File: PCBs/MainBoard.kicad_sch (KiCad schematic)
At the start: 46 parts, among them IC1 PASCO2V01BUMA1, J1 USB_C_Receptacle, J2 Conn_01x12_FPC_0.5mm, J3 Qwiic_RA, J4 SM06B-GHS-TB, SW1 PTH_RA_h7.5mm, SW2 SMD_4.6x2.8mm_h2.5mm, SW3 SMD_4.6x2.8mm_h2.5mm, U1 TVS_ESD_USB, U2 ESP32-S3-MINI, U3 AP3012, U4 AP2112K-3.3

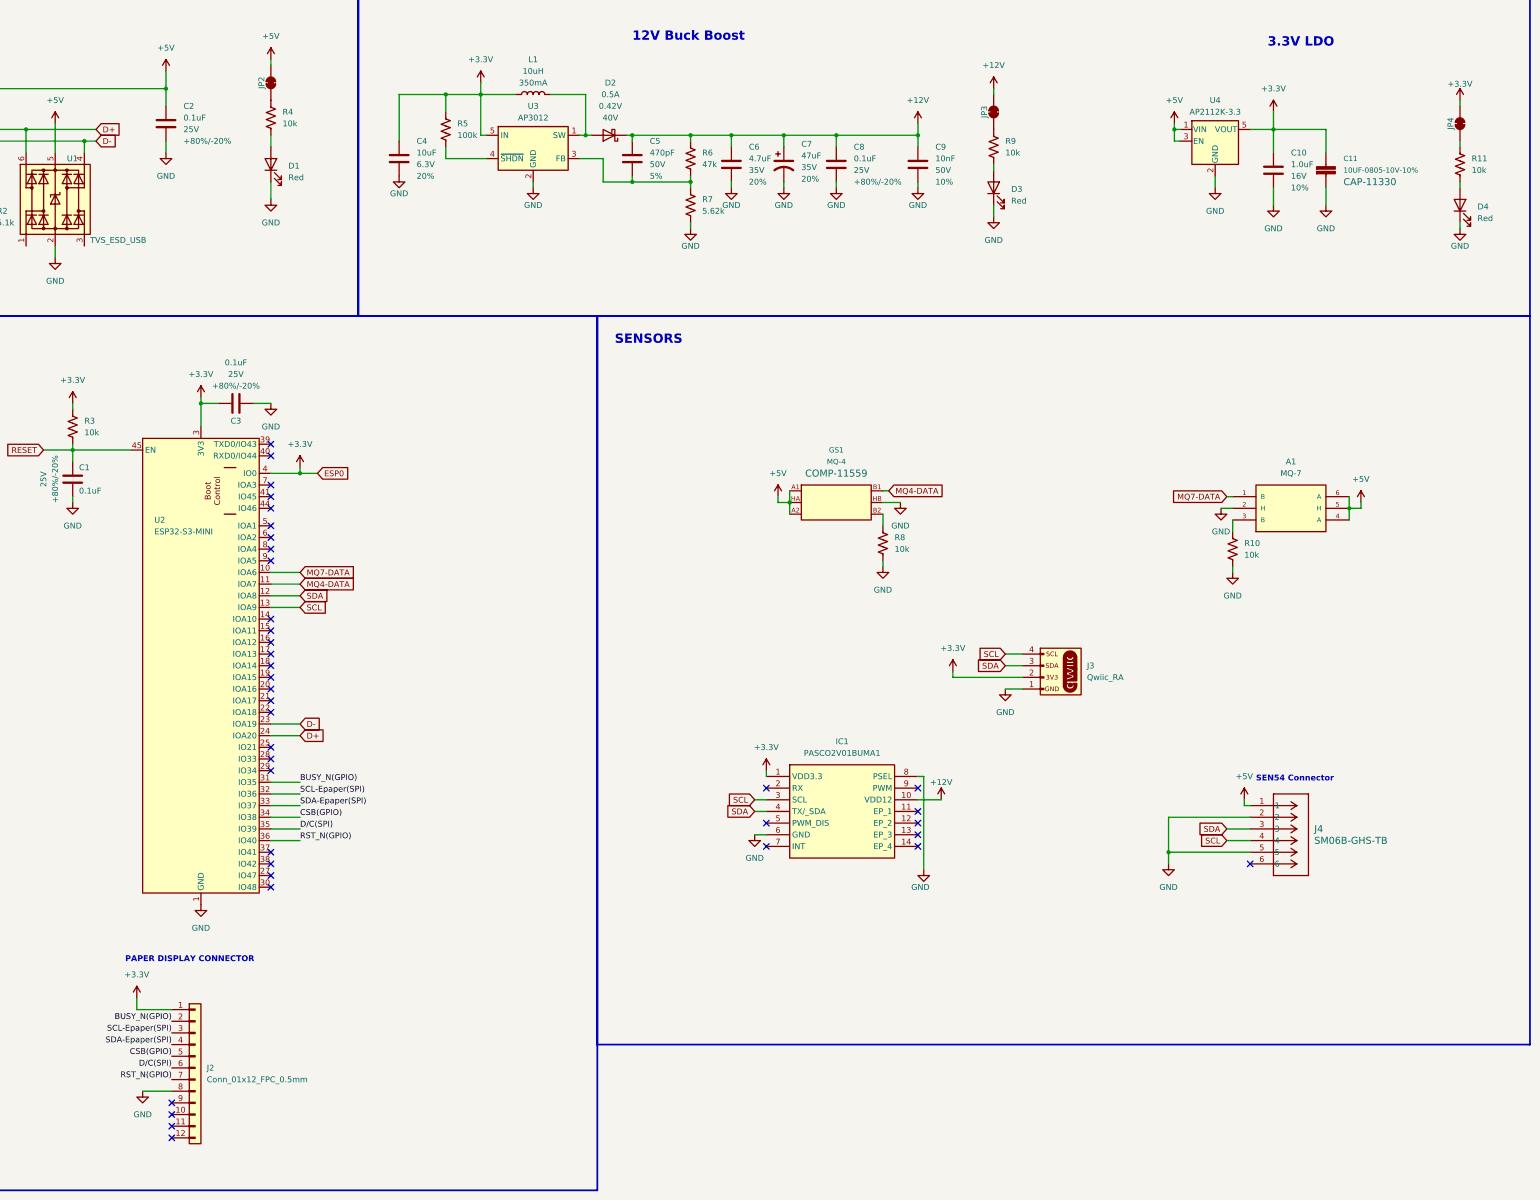
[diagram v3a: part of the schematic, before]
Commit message: More updates
Working from google doc review - replaced all net labels with global labels - added debounce capacitors - removed all 0402 components and replaced with 0603 components - line "tidy up" - see google doc for additional comments and work done :)
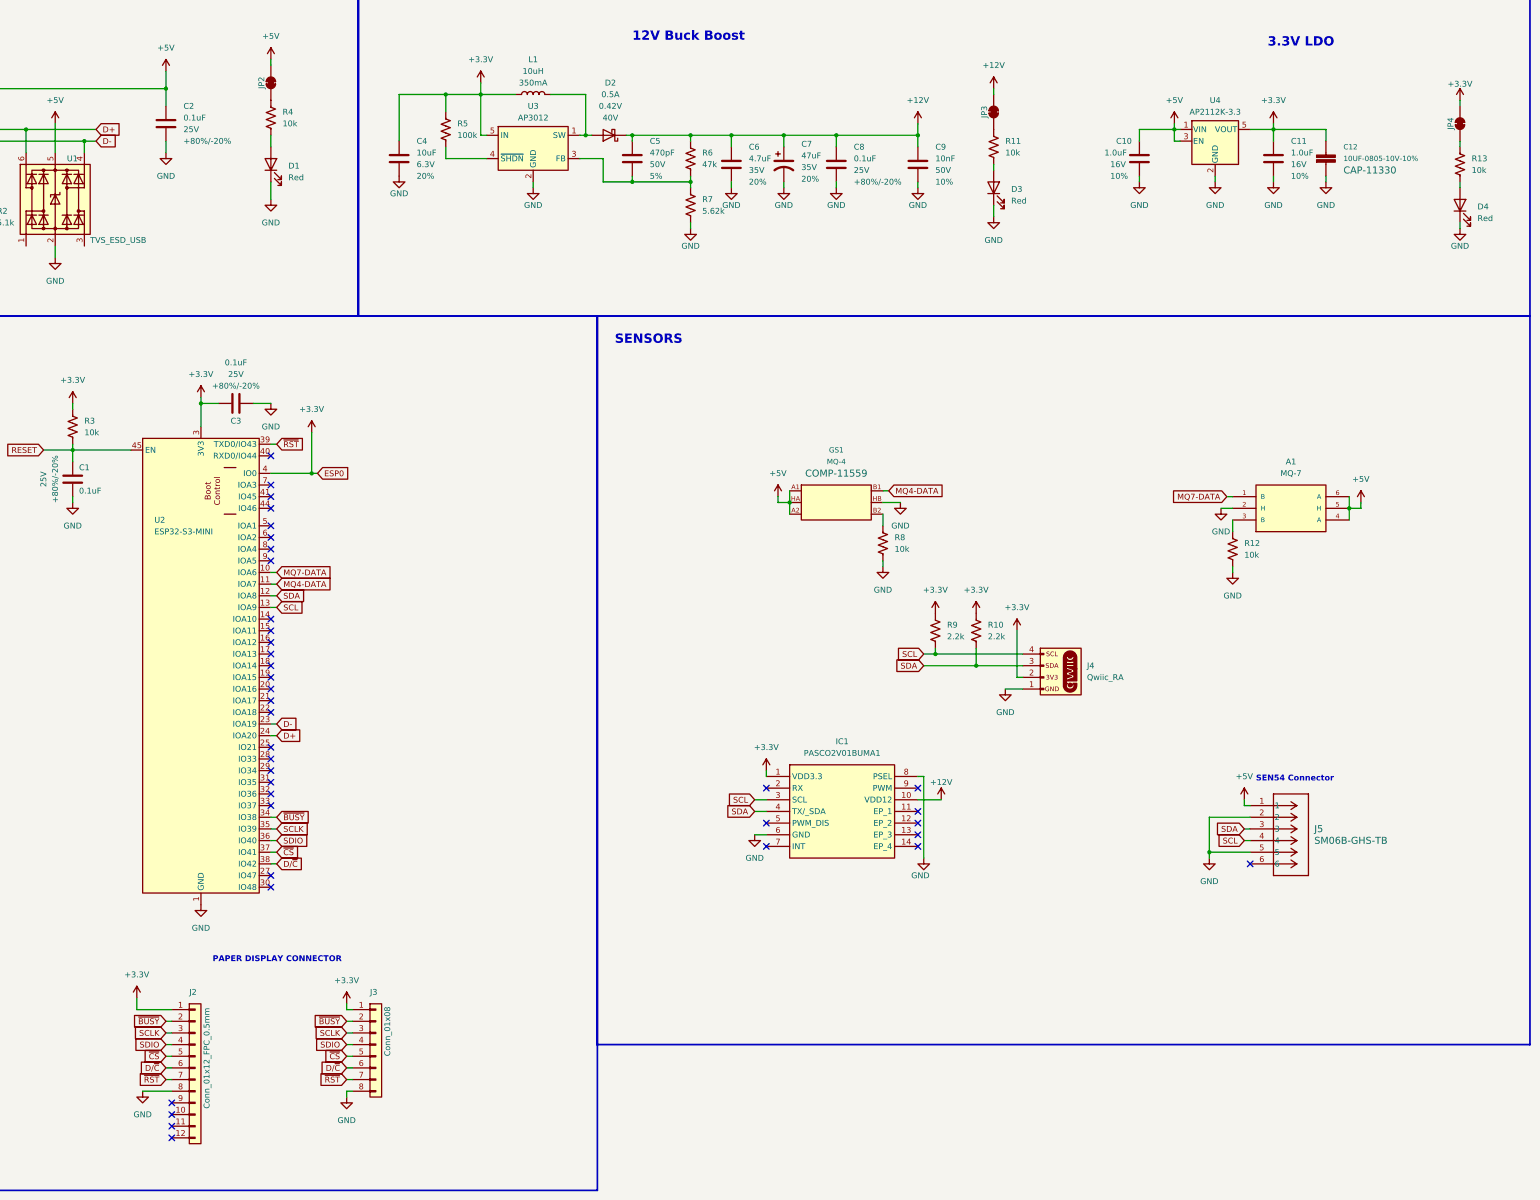
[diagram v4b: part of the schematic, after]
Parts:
- added C10: 1.0uF, SparkFun-Capacitor:C_0402_1005Metric, symbol SparkFun-Capacitor:1.0uF_0402_16V_10%
- added J3: Conn_01x08, SparkFun-Connector:1X08, symbol SparkFun-Connector:Conn_01x08
- added R10, R9: 2.2k, SparkFun-Resistor:R_0603_1608Metric, symbol SparkFun-Resistor:2.2k_0603
- renumbered C10 to C11, C11 to C12, J3 to J4, J4 to J5, R9 to R11, R10 to R12, R11 to R13
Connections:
- net +3.3V: now also J3.1 (Pin_1), R10.1, R9.1
- net +5V: now also C10.2
- net GND: now also C10.1, J3.8 (Pin_8)
- net SCL: now also R9.2
- net SDA: now also R10.2
- net ~{CS}: now reaches U2.37 (IO41)
- net ~{CS}: now also J2.5 (Pin_5), J3.5 (Pin_5)
- net D/~{C}: now reaches U2.38 (IO42)
- net D/~{C}: now also J2.6 (Pin_6), J3.6 (Pin_6)
- net ~{RST}: now reaches U2.39 (TXD0/IO43)
- net ~{RST}: now also J2.7 (Pin_7), J3.7 (Pin_7)
- net BUSY_N(GPIO): no longer names the net of U2.31 (IO35)
- net BUSY_N(GPIO): no longer J2.2 (Pin_2)
- net CSB(GPIO) renamed ~{BUSY}
- net ~{BUSY}: now also J2.2 (Pin_2), J3.2 (Pin_2); no longer J2.5 (Pin_5)
- net D/C(SPI) renamed SCLK
- net SCLK: now also J2.3 (Pin_3), J3.3 (Pin_3); no longer J2.6 (Pin_6)
- net RST_N(GPIO) renamed SDIO
- net SDIO: now also J2.4 (Pin_4), J3.4 (Pin_4); no longer J2.7 (Pin_7)
- net SCL-Epaper(SPI): no longer names the net of U2.32 (IO36)
- net SCL-Epaper(SPI): no longer J2.3 (Pin_3)
- net SDA-Epaper(SPI): no longer names the net of U2.33 (IO37)
- net SDA-Epaper(SPI): no longer J2.4 (Pin_4)
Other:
- moved on the sheet: C11, C12

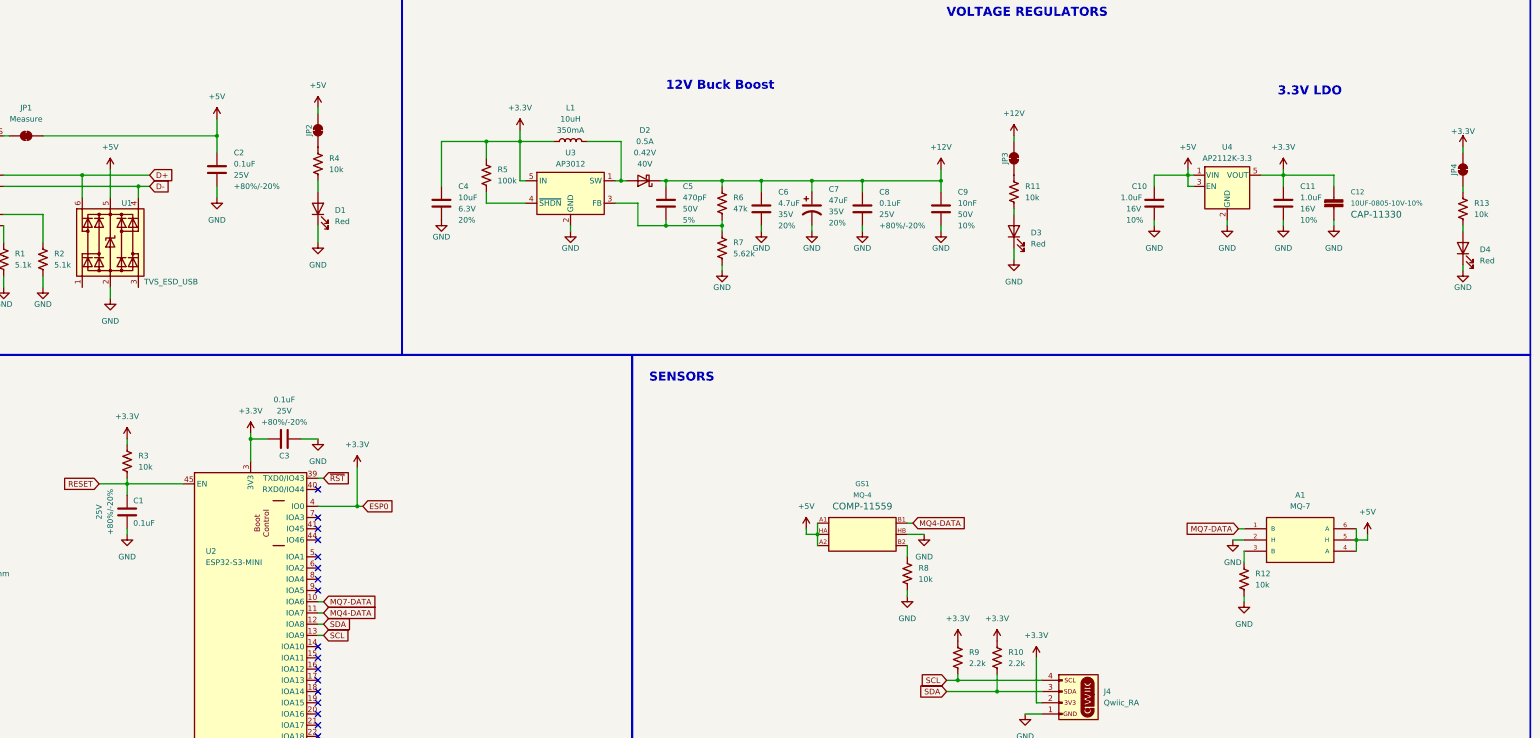
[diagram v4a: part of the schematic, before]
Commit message: Main Board Update
Fixed ESP0 power rail issue
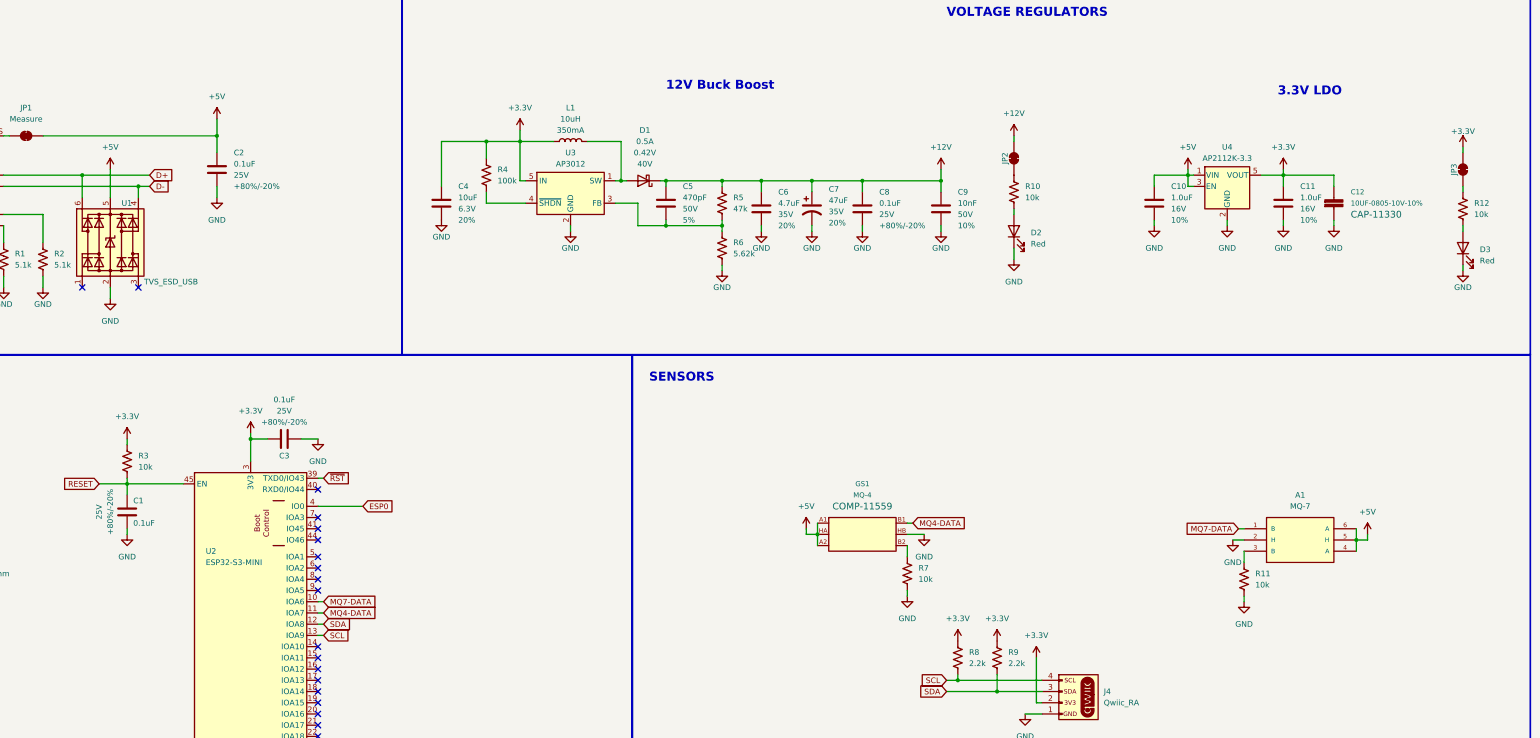
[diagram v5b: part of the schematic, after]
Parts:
- removed C10: 1.0uF, SparkFun-Capacitor:C_0402_1005Metric, symbol SparkFun-Capacitor:1.0uF_0402_16V_10%
- removed D1: Red, SparkFun-LED:LED_0603_1608Metric, symbol SparkFun-LED:LED_Red_0603
- removed JP2: ~, SparkFun-Jumper:SMT-JUMPER_2_NC_TRACE_SILK, symbol SparkFun-Jumper:SolderJumper_2_Bridged
- removed R4: 10k, SparkFun-Resistor:R_0603_1608Metric, symbol SparkFun-Resistor:10k_0603
- added C10: 1.0uF, SparkFun-Capacitor:C_0603_1608Metric, symbol SparkFun-Capacitor:1.0uF_0603_16V_10%
- renumbered D2 to D1, D3 to D2, D4 to D3, JP3 to JP2, JP4 to JP3, R11 to R10, R12 to R11, R13 to R12, R5 to R4, R6 to R5, R7 to R6, R8 to R7, R9 to R8, R10 to R9
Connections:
- net +3.3V: no longer SW3.2 (B), U2.4 (IO0)
- net +5V: now also C10.1
- net GND: now also C10.2
- new net ESP0: SW3.2 (B), U2.4 (IO0)
- no-connect marks 38 -> 40

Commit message: Updates From feedback
Added new MQ sensors and PAS CO2 sensors - Added more from board review notes on google doc
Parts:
- removed A1: MQ-7, MQ-7:XDCR_MQ-7, symbol MQ-7:MQ-7
- removed C12: 10UF-0805-10V-10%, 0805, symbol SparkFun-Capacitors:10UF-0805-10V-10%
- removed GS1: MQ-4, GAS_SENSOR, symbol SparkFun-Sensors:GAS_SENSORMQ-4
- removed IC1: PASCO2V01BUMA1, PASCO2V01BUMA1, symbol PASCO2V01BUMA1:PASCO2V01BUMA1
- removed R11, R7: 10k, SparkFun-Resistor:R_0603_1608Metric, symbol SparkFun-Resistor:10k_0603
- added C12: 10uF, SparkFun-Capacitor:C_0603_1608Metric, symbol SparkFun-Capacitor:10uF_0603_6.3V_20%
- added R11, R7: 4.7k, SparkFun-Resistor:R_0603_1608Metric, symbol SparkFun-Resistor:4.7k_0603
- added U4: MQ-4 Gas Sensor, SparkFun-Sensor:MQ-4 Gas Sensor, symbol SparkFun-Sensor:MQ-4 Gas Sensor
- added U5: PASCO2V01BUMA1, SparkFun-Sensor:LG-MLGA-14-1_Z8B00206105, symbol SparkFun-Sensor:PASCO2V01BUMA1
- added U7: MQ-7 Gas Sensor, SparkFun-Sensor:MQ-7 Gas Sensor, symbol SparkFun-Sensor:MQ-7 Gas Sensor
- renumbered R9 to R10, R10 to R9, U4 to U6
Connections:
- net +12V: now also U5.10 (12V)
- net +3.3V: now also R4.2, C12.1, U5.1 (3V3); no longer R4.1
- net +5V: now also U4.2 (5V), U7.2 (VCC)
- net GND: now also C12.2, R11.2, R7.2, U4.4 (SENSE-GND), U4.5 (GND), U4.6 (SENSE-GND), U5.11 (GND), U5.12 (GND), U5.13 (GND), U5.14 (GND), U5.5 (PWM_DIS), U5.6 (GND), U5.8 (PSEL), U7.4 (SENSE-GND), U7.5 (GND), U7.6 (SENSE-GND)
- net SCL: now also U5.3 (SCL)
- net SDA: now also U5.4 (SDA/TX)
- net ~{SHDN}-EN: now reaches U3.4 (~{SHDN})
- net ~{SHDN}-EN: now also R4.1, U2.22 (IOA18); no longer R4.2
- net CO2_INT: now reaches U2.15 (IOA11)
- net CO2_INT: now also U5.7 (INT)
- net MQ4-DATA renamed ESP11/MQ4
- net ESP11/MQ4: now also R7.1, U4.1 (SENSE), U4.3 (SENSE)
- net MQ7-DATA renamed ESP10/MQ7
- net ESP10/MQ7: now also R11.1, U7.1 (SENSE), U7.3 (SENSE)
- no-connect marks 40 -> 32
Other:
- note added: "EXTERNAL RESET BUTTON"
- note added: "SEN54 CONNECTOR"
- note added: "USB-C INTERFACE"
- note removed: "External Reset Button"
- note removed: "SEN54 Connector"
- note removed: "USB INTERFACE"
- title: (none) -> SparkFun Home Air Quality Sensor - Main PCB
- moved on the sheet: C5, C6, C7, C8, C9, D1, D2, J4, JP2, L1, R10, R5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

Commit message: fuck you
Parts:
- removed J5: SM06B-GHS-TB, CONN_SM06B-GHS-TB_JST, symbol SM06B-GHS-TB:SM06B-GHS-TB
- added C13, C14: 10uF, SparkFun-Capacitor:C_0603_1608Metric, symbol SparkFun-Capacitor:10uF_0603_10V_20%
- added FID1, FID2, FID3, FID4: Fiducial_0.5mm, SparkFun-Aesthetic:Fiducial_0.5mm_Mask1mm, symbol SparkFun-Aesthetic:Fiducial_0.5mm
- added G2: SparkFun_Logo, symbol SparkFun-Aesthetic:SparkFun_Logo
- added Q1: AO3404A, SparkFun-Semiconductor-Standard:SOT23-3, symbol SparkFun-DiscreteSemi:Q_NMOS_5.8A_30V
- added R13: 10k, SparkFun-Resistor:R_0603_1608Metric, symbol SparkFun-Resistor:10k_0603
- added R14: 1k, SparkFun-Resistor:R_0603_1608Metric, symbol SparkFun-Resistor:1k_0603
- added ST1: Stand_off, SparkFun-Hardware:STAND-OFF, symbol SparkFun-Hardware:Stand_off
- added U8: SEN55, SparkFun-Connector:JST-6-SMD-1.25MM-LOCKING, symbol SparkFun-Sensor:SEN55
- added U9: MQ-7 Gas Sensor, SparkFun-Sensor:MQ-7 Gas Sensor, symbol SparkFun-Sensor:MQ-7_Gas_Sensor_-_Full_Pinout
- J2: PROD_ID (none) -> CONN-15766
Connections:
- net +5V: now also U8.1 (VDD), U9.4 (GND), U9.6 (GND)
- net D/~{C}: now also J2.4 (Pin_4), J3.4 (Pin_4), U2.36 (IO40); no longer J2.6 (Pin_6), J3.6 (Pin_6), U2.38 (IO42)
- net GND: now also R13.2, U8.2 (GND), U8.5 (SEL)
- net SCL: now also U8.4 (SCL)
- net SCLK: now also J2.6 (Pin_6), J3.6 (Pin_6), U2.38 (IO42); no longer J2.3 (Pin_3), J3.3 (Pin_3), U2.35 (IO39)
- net SDA: now also U8.3 (SDA)
- net SDIO: now also J2.7 (Pin_7), J3.7 (Pin_7), U2.39 (TXD0/IO43); no longer J2.4 (Pin_4), J3.4 (Pin_4), U2.36 (IO40)
- net ~{RST}: now also J2.3 (Pin_3), J3.3 (Pin_3), U2.35 (IO39); no longer J2.7 (Pin_7), J3.7 (Pin_7), U2.39 (TXD0/IO43)
- new net: R13.1, U9.1 (SENSE), U9.3 (SENSE)
- no-connect marks 32 -> 31
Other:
- note added: "CO SENSOR"
- note added: "Fiducials"
- note added: "METHANE SENSOR"
- note added: "PASCO2 CIRCUIT"
- note added: "QWIIC CONNECTOR CIRCUIT"
- note added: "SEN55 CONNECTOR"
- note added: "Stand Off"
- note added: "Topside Right Topside left Bottomside Right Bottomside left"
- note removed: "SEN54 CONNECTOR"
- moved on the sheet: R11, U7
